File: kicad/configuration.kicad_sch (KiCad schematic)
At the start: 15 parts, among them U1 MIMXRT1171DVMAB, U3 W25Q64JWUUIQ

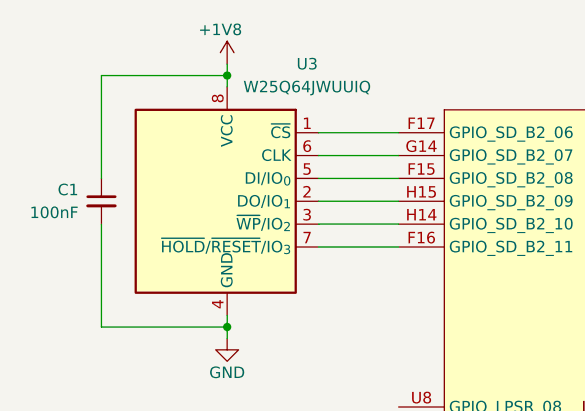
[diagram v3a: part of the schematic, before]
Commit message: added magnetometer to schematic
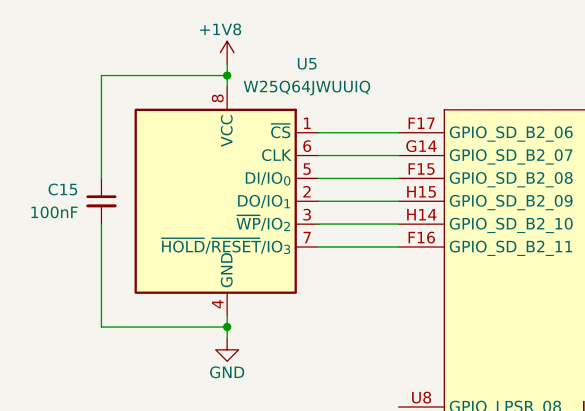
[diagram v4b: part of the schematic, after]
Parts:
- renumbered C1 to C15, U3 to U5
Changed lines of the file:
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@@
 		(in_pos_files yes)
 		(dnp no)
-		(property "Reference" "U3"
+		(property "Reference" "U5"
 			(at 124.46 96.52 0)
 			(show_name no)
@@
 			(project "DEV-G2-NANO"
 				(path "/b6656e4d-fdee-4b90-a905-7068c060191f/45e1da5b-d52f-4e94-b563-4995febadb51"
-					(reference "U3")
+					(reference "U5")
 					(unit 1)
 				)
@@
 		(in_pos_files yes)
 		(dnp no)
-		(property "Reference" "#PWR010"
+		(property "Reference" "#PWR022"
 			(at 115.57 133.35 0)
 			(hide yes)
@@
 			(project "DEV-G2-NANO"
 				(path "/b6656e4d-fdee-4b90-a905-7068c060191f/45e1da5b-d52f-4e94-b563-4995febadb51"
-					(reference "#PWR010")
+					(reference "#PWR022")
 					(unit 1)
 				)
@@
 		(in_pos_files yes)
 		(dnp no)
-		(property "Reference" "#PWR09"
+		(property "Reference" "#PWR021"
 			(at 115.57 100.33 0)
 			(hide yes)
@@
 			(project "DEV-G2-NANO"
 				(path "/b6656e4d-fdee-4b90-a905-7068c060191f/45e1da5b-d52f-4e94-b563-4995febadb51"
-					(reference "#PWR09")
+					(reference "#PWR021")
 					(unit 1)
 				)
@@
 		(in_pos_files yes)
 		(dnp no)
-		(property "Reference" "#PWR011"
+		(property "Reference" "#PWR024"
 			(at 220.98 143.51 0)
 			(hide yes)
@@
 			(project "DEV-G2-NANO"
 				(path "/b6656e4d-fdee-4b90-a905-7068c060191f/45e1da5b-d52f-4e94-b563-4995febadb51"
-					(reference "#PWR011")
+					(reference "#PWR024")
 					(unit 1)
 				)
@@
 		(in_pos_files yes)
 		(dnp no)
-		(property "Reference" "#PWR012"
+		(property "Reference" "#PWR023"
 			(at 234.95 139.7 0)
 			(hide yes)
@@
 			(project "DEV-G2-NANO"
 				(path "/b6656e4d-fdee-4b90-a905-7068c060191f/45e1da5b-d52f-4e94-b563-4995febadb51"
-					(reference "#PWR012")
+					(reference "#PWR023")
 					(unit 1)
 				)
@@
 		(in_pos_files yes)
 		(dnp no)
-		(property "Reference" "C1"
+		(property "Reference" "C15"
 			(at 99.06 110.4962 0)
 			(show_name no)
@@
 			(project "DEV-G2-NANO"
 				(path "/b6656e4d-fdee-4b90-a905-7068c060191f/45e1da5b-d52f-4e94-b563-4995febadb51"
-					(reference "C1")
+					(reference "C15")
 					(unit 1)
 				)

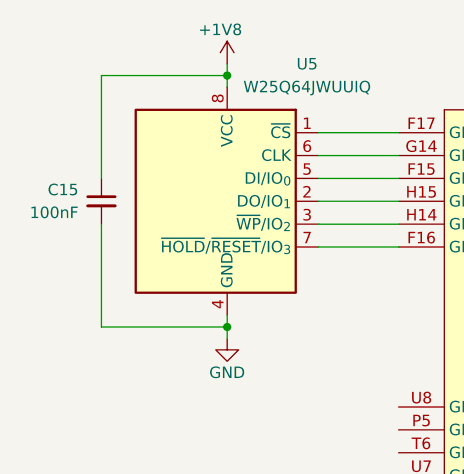
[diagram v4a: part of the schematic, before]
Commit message: added bypass caps
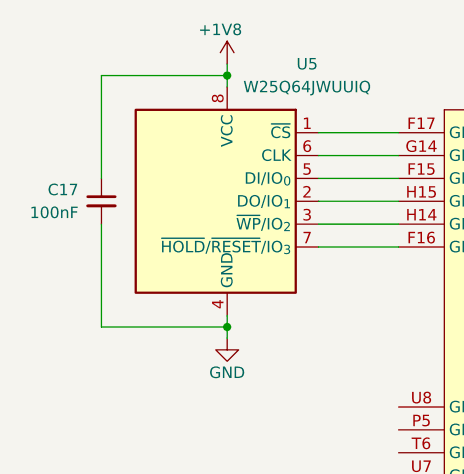
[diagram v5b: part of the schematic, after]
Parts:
- renumbered C15 to C17
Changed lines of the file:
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@@
 		(in_pos_files yes)
 		(dnp no)
-		(property "Reference" "#PWR022"
+		(property "Reference" "#PWR026"
 			(at 115.57 133.35 0)
 			(hide yes)
@@
 			(project "DEV-G2-NANO"
 				(path "/b6656e4d-fdee-4b90-a905-7068c060191f/45e1da5b-d52f-4e94-b563-4995febadb51"
-					(reference "#PWR022")
+					(reference "#PWR026")
 					(unit 1)
 				)
@@
 		(in_pos_files yes)
 		(dnp no)
-		(property "Reference" "#PWR021"
+		(property "Reference" "#PWR025"
 			(at 115.57 100.33 0)
 			(hide yes)
@@
 			(project "DEV-G2-NANO"
 				(path "/b6656e4d-fdee-4b90-a905-7068c060191f/45e1da5b-d52f-4e94-b563-4995febadb51"
-					(reference "#PWR021")
+					(reference "#PWR025")
 					(unit 1)
 				)
@@
 		(in_pos_files yes)
 		(dnp no)
-		(property "Reference" "#PWR024"
+		(property "Reference" "#PWR028"
 			(at 220.98 143.51 0)
 			(hide yes)
@@
 			(project "DEV-G2-NANO"
 				(path "/b6656e4d-fdee-4b90-a905-7068c060191f/45e1da5b-d52f-4e94-b563-4995febadb51"
-					(reference "#PWR024")
+					(reference "#PWR028")
 					(unit 1)
 				)
@@
 		(in_pos_files yes)
 		(dnp no)
-		(property "Reference" "#PWR023"
+		(property "Reference" "#PWR027"
 			(at 234.95 139.7 0)
 			(hide yes)
@@
 			(project "DEV-G2-NANO"
 				(path "/b6656e4d-fdee-4b90-a905-7068c060191f/45e1da5b-d52f-4e94-b563-4995febadb51"
-					(reference "#PWR023")
+					(reference "#PWR027")
 					(unit 1)
 				)
@@
 		(in_pos_files yes)
 		(dnp no)
-		(property "Reference" "C15"
+		(property "Reference" "C17"
 			(at 99.06 110.4962 0)
 			(show_name no)
@@
 			(project "DEV-G2-NANO"
 				(path "/b6656e4d-fdee-4b90-a905-7068c060191f/45e1da5b-d52f-4e94-b563-4995febadb51"
-					(reference "C15")
+					(reference "C17")
 					(unit 1)
 				)

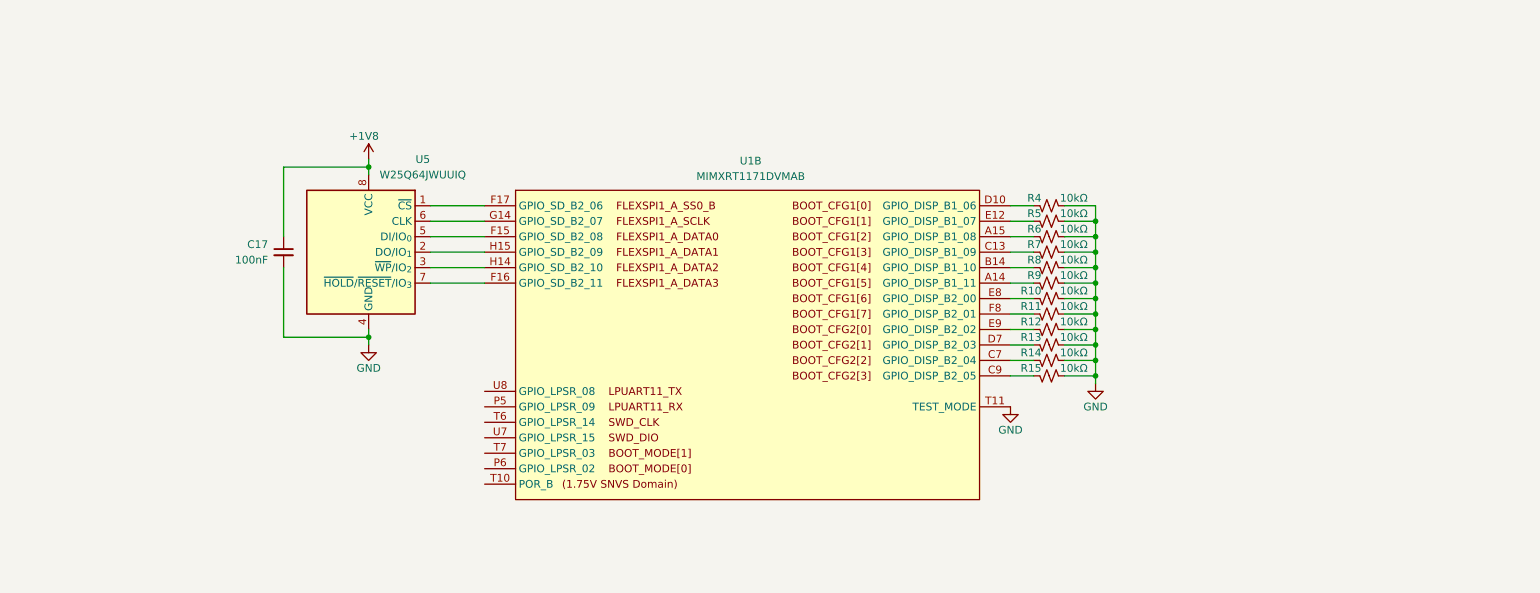
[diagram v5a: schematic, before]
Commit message: added KL26 (DAPLink HIC) to schematic
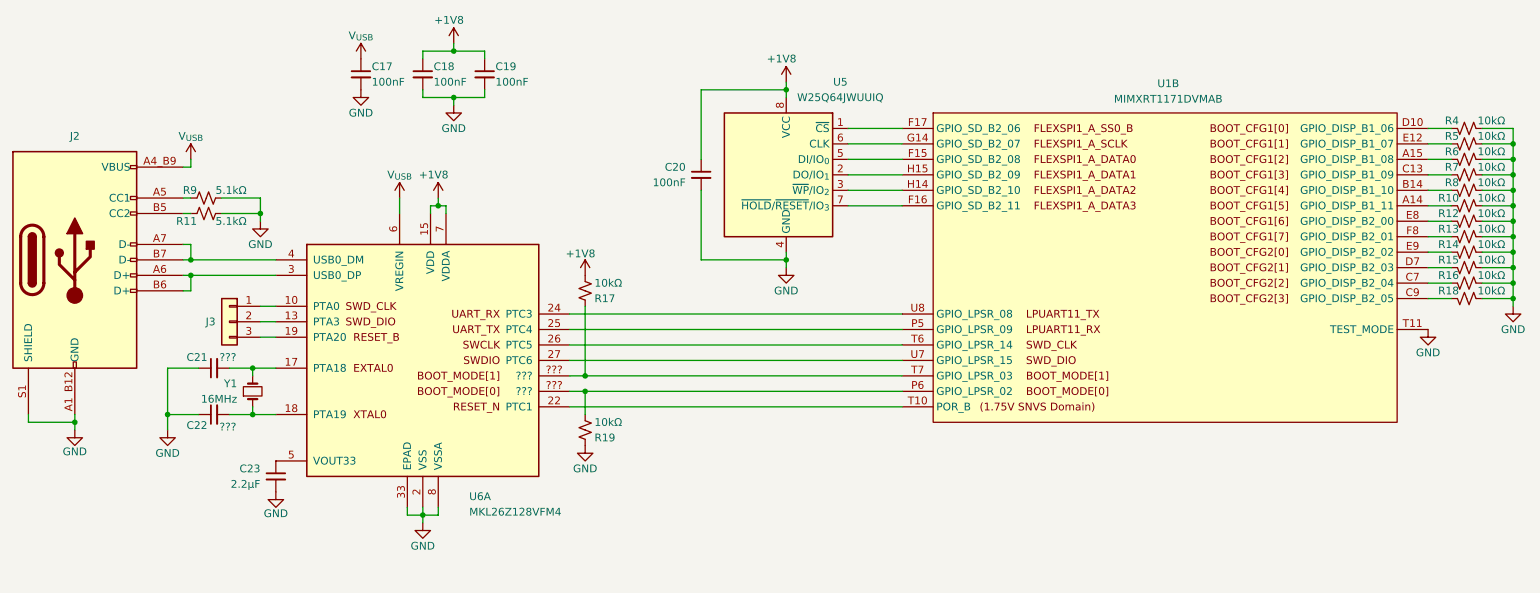
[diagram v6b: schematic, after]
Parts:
- added C17, C18, C19: 100nF, symbol Device:C_Small
- added C21, C22: ???, symbol Device:C_Small
- added C23: 2.2µF, symbol Device:C_Small
- added J2: GSB1C41110SSHR, -- project_footprints --:USB_C, symbol -- project_symbols --:USB C
- added J3: HIC_SWD, symbol Connector_Generic:Conn_01x03
- added R11, R9: 5.1kΩ, symbol Device:R_Small_US
- added R17, R19: 10kΩ, symbol Device:R_Small_US
- added U6: MKL26Z128VFM4, Package_DFN_QFN:QFN-32-1EP_5x5mm_P0.5mm_EP3.45x3.45mm, symbol project_symbols:MKL26Z128VFM4
- added Y1: 16MHz, symbol Device:Crystal_Small
- renumbered C17 to C20, R9 to R10, R10 to R12, R11 to R13, R12 to R14, R13 to R15, R14 to R16, R15 to R18
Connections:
- net +1V8: now also C18.1, C19.1, R17.2, U6.15 (VDD), U6.7 (VDDA)
- net GND: now also C17.2, C18.2, C19.2, C21.1, C22.1, C23.2, J2.A1_B12 (GND), J2.B1_A12 (GND), J2.S1 (SHIELD), R11.2, R19.1, R9.2, U6.16 (VSS), U6.2 (VSS), U6.33 (EPAD), U6.8 (VSSA)
- net at U1.P5 (GPIO_LPSR_09): now also U6.25 (PTC4)
- net at U1.P6 (GPIO_LPSR_02): now also R19.2, U6.???
- net at U1.T10 (POR_B): now also U6.22 (PTC1)
- net at U1.T6 (GPIO_LPSR_14): now also U6.26 (PTC5)
- net at U1.T7 (GPIO_LPSR_03): now also R17.1, U6.???
- net at U1.U7 (GPIO_LPSR_15): now also U6.27 (PTC6)
- net at U1.U8 (GPIO_LPSR_08): now also U6.24 (PTC3)
- new net: C22.2, U6.18 (PTA19), Y1.1
- new net: C21.2, U6.17 (PTA18), Y1.2
- new net: J2.A5 (CC1), R9.1
- new net: J2.A6 (D+), J2.B6 (D+), U6.3 (USB0_DP)
- new net: J2.A7 (D-), J2.B7 (D-), U6.4 (USB0_DM)
- new net: J2.B5 (CC2), R11.1
- new net: J3.1 (Pin_1), U6.10 (PTA0)
- new net: J3.2 (Pin_2), U6.13 (PTA3)
- new net: J3.3 (Pin_3), U6.19 (PTA20)
- new net: C23.1, U6.5 (VOUT33)
- new net V_{USB}: C17.1, J2.A4_B9 (VBUS), J2.B4_A9 (VBUS), U6.6 (VREGIN)
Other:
- moved on the sheet: C20, R10, R12, R13, R14, R15, R16, R18, R4, R5, R6, R7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

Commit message: added RTMC-G2-4IQ48 to schematic
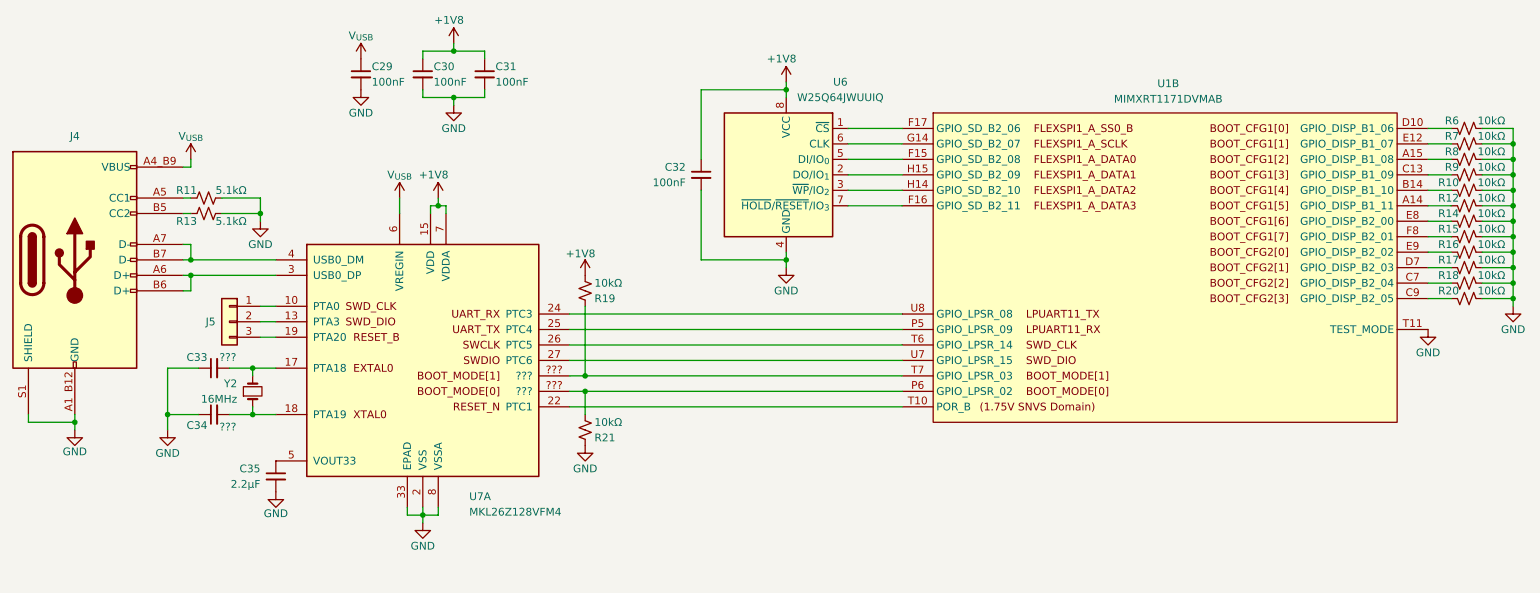
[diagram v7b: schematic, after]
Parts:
- renumbered C17 to C29, C18 to C30, C19 to C31, C20 to C32, C21 to C33, C22 to C34, C23 to C35, J2 to J4, J3 to J5, R8 to R10, R9 to R11, R10 to R12, R11 to R13, R12 to R14, R13 to R15, R14 to R16, R15 to R17, R16 to R18, R17 to R19, R18 to R20, R19 to R21, R4 to R6, R5 to R7, R6 to R8, R7 to R9, U5 to U6, U6 to U7, Y1 to Y2

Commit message: added several footprints
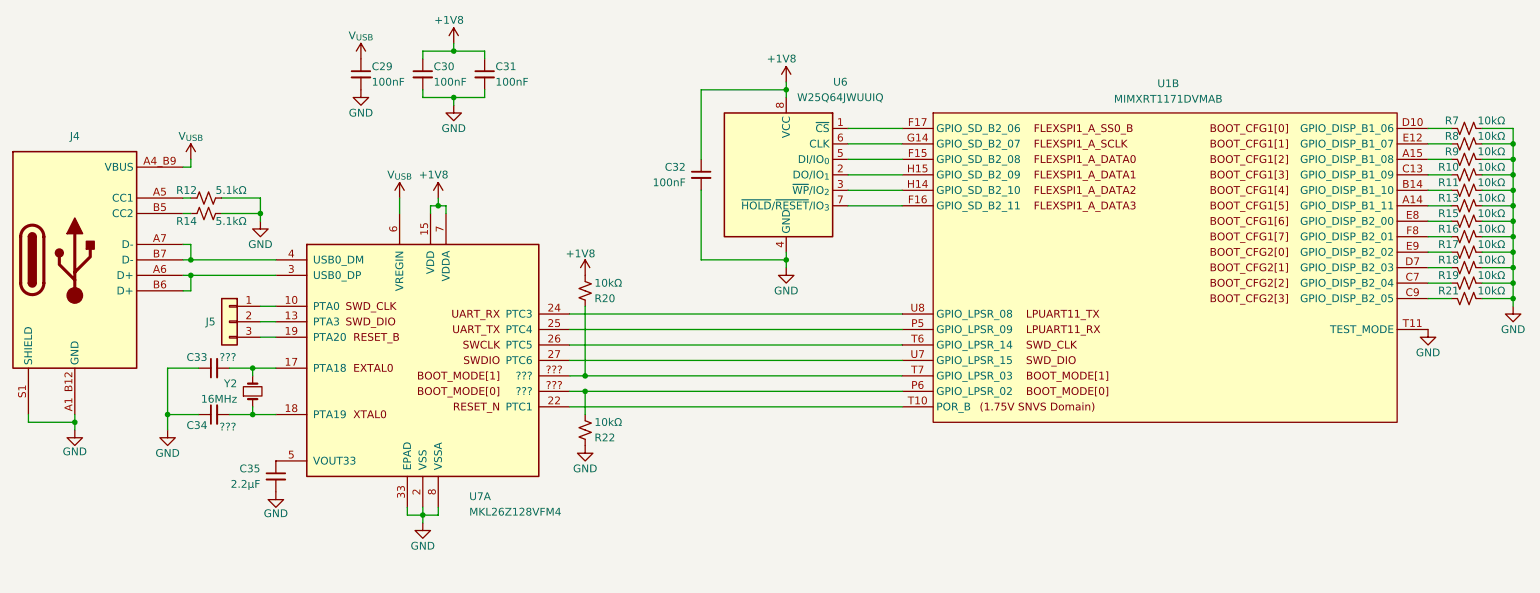
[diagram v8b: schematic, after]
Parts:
- removed J4: GSB1C41110SSHR, -- project_footprints --:USB_C, symbol -- project_symbols --:USB C
- added J4: (no value), project_footprints:UJ20-C-H-G-SMT-5-P16, symbol project_symbols:USB-C
- C29, C30, C31, C32: footprint (none) -> Capacitor_SMD:C_0201_0603Metric
- J5: value HIC_SWD -> (none); footprint (none) -> project_footprints:TestPoints-3
- R10: renamed from R9; footprint (none) -> Resistor_SMD:R_0201_0603Metric
- R11: renamed from R10; footprint (none) -> Resistor_SMD:R_0201_0603Metric
- R12: renamed from R11; footprint (none) -> Resistor_SMD:R_0201_0603Metric
- R13: renamed from R12; footprint (none) -> Resistor_SMD:R_0201_0603Metric
- R14: renamed from R13; footprint (none) -> Resistor_SMD:R_0201_0603Metric
- R15: renamed from R14; footprint (none) -> Resistor_SMD:R_0201_0603Metric
- R16: renamed from R15; footprint (none) -> Resistor_SMD:R_0201_0603Metric
- R17: renamed from R16; footprint (none) -> Resistor_SMD:R_0201_0603Metric
- R18: renamed from R17; footprint (none) -> Resistor_SMD:R_0201_0603Metric
- R19: renamed from R18; footprint (none) -> Resistor_SMD:R_0201_0603Metric
- R20: renamed from R19; footprint (none) -> Resistor_SMD:R_0201_0603Metric
- R21: renamed from R20; footprint (none) -> Resistor_SMD:R_0201_0603Metric
- R22: renamed from R21; footprint (none) -> Resistor_SMD:R_0201_0603Metric
- R7: renamed from R6; footprint (none) -> Resistor_SMD:R_0201_0603Metric
- R8: renamed from R7; footprint (none) -> Resistor_SMD:R_0201_0603Metric
- R9: renamed from R8; footprint (none) -> Resistor_SMD:R_0201_0603Metric
- U1: footprint Package_BGA:MAPBGA-289_14x14mm_Layout17x17_P0.8mm -> project_footprints:MIMXRT1171DVMAB
- U6: footprint (none) -> project_footprints:W25Q64JWUUIQ
- U7: footprint Package_DFN_QFN:QFN-32-1EP_5x5mm_P0.5mm_EP3.45x3.45mm -> project_footprints:MKL26Z128VFM4
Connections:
- net GND: now also J4.A1_B12 (GND), J4.B1_A12 (GND), J4.S1 (SHIELD)
- net V_{USB}: now also J4.A4_B9 (VBUS), J4.B4_A9 (VBUS)
- net at R12.1: now also J4.A5 (CC1)
- net at U7.3 (USB0_DP): now also J4.A6 (D+), J4.B6 (D+)
- net at U7.4 (USB0_DM): now also J4.A7 (D-), J4.B7 (D-)
- net at R14.1: now also J4.B5 (CC2)
